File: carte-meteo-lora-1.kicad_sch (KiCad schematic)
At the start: 52 parts, among them J2 USB_C_Receptacle_USB2.0_14P, J3 Conn_01x04, J4 Conn_01x04_Pin, J5 Conn_01x04, U1 MS5607-02BA, U3 HS96L03W2C03, U4 GXHT30, U6 ESP32-C5, U7 HTU21, Y1 48M

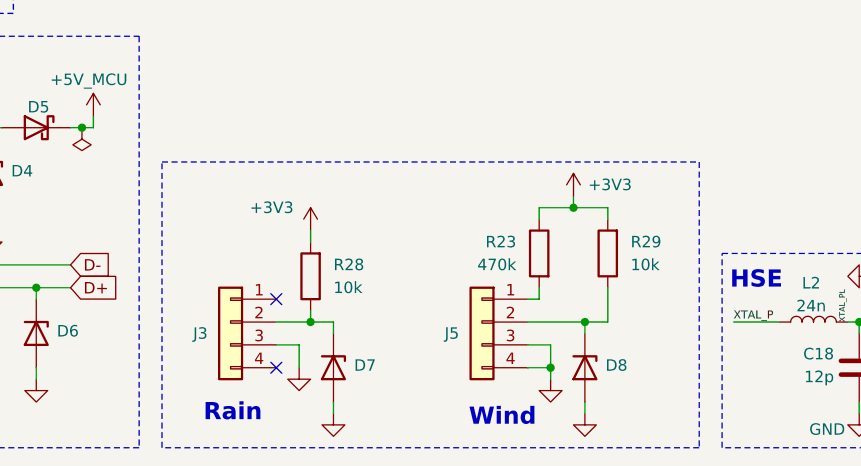
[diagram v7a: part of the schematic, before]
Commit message: schem: improve rain and wind connectors
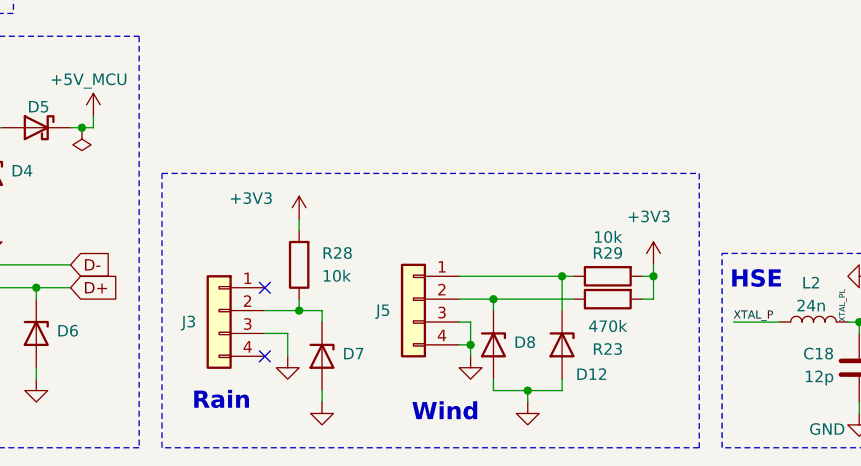
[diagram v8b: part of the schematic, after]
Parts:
- added D12: H5VU10U, GLCS:Diode_DFN1006, symbol GLCS:H5VU10U
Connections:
- net +3V3: now also R23.2; no longer R23.1
- net GND: now also D12.2 (A)
- net at D8.1 (K), J5.2 (Pin_2): now also R23.1; no longer R29.1
- net at J5.1 (Pin_1): now also R29.1, D12.1 (K); no longer R23.2
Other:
- moved on the sheet: J3, J5, R28
